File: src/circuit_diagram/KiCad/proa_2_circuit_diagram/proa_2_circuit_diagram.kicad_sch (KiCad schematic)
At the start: 29 parts, among them U1 BUCK_48V_24V_10A, U2 BUCK_24V_5V_5A, U3 ADS1115IDGS, U5 TCA9800

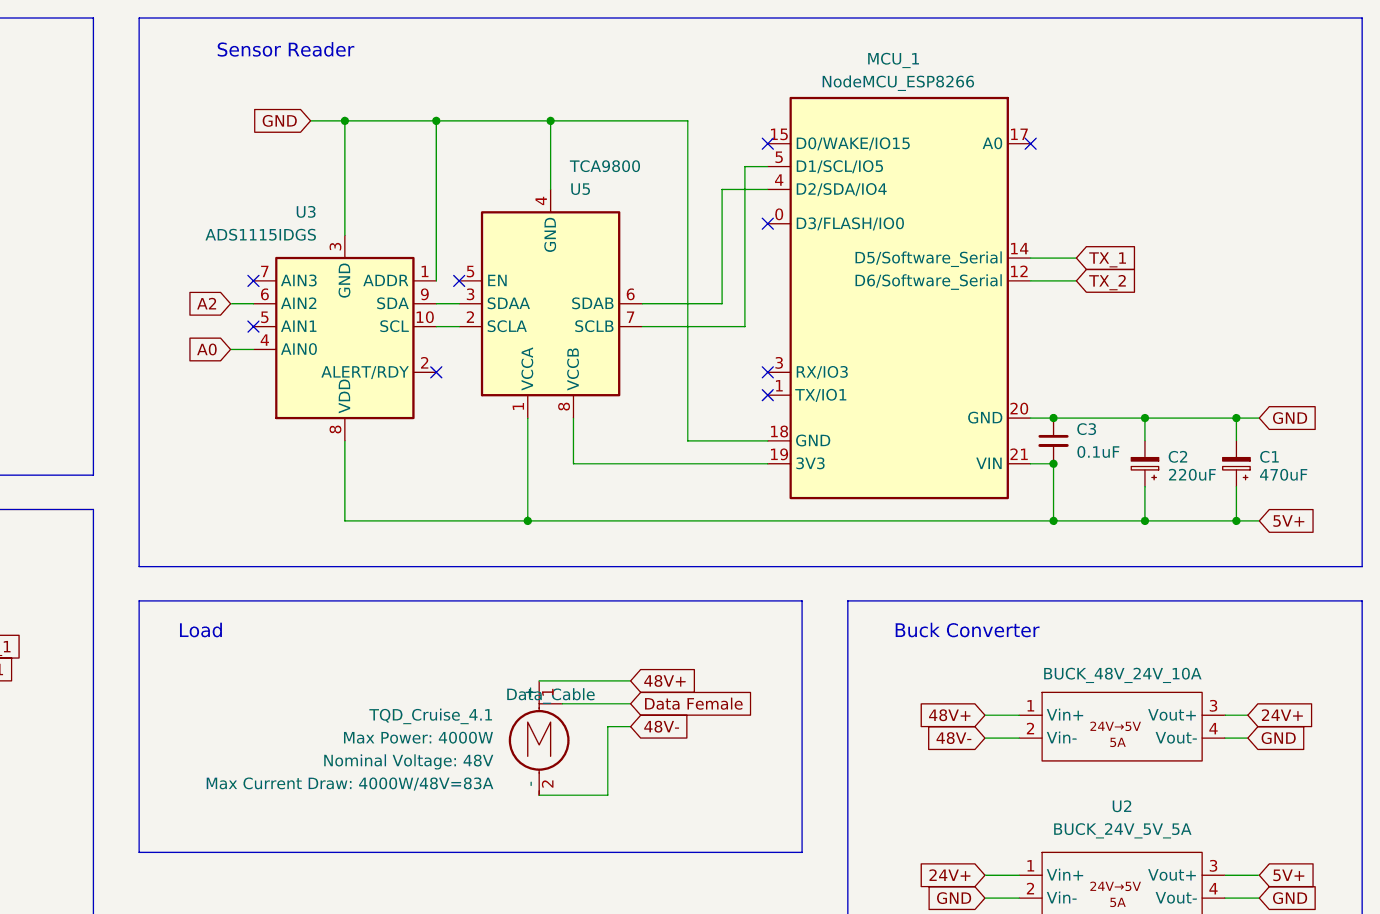
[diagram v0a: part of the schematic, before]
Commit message: Reroute electrical constant file import
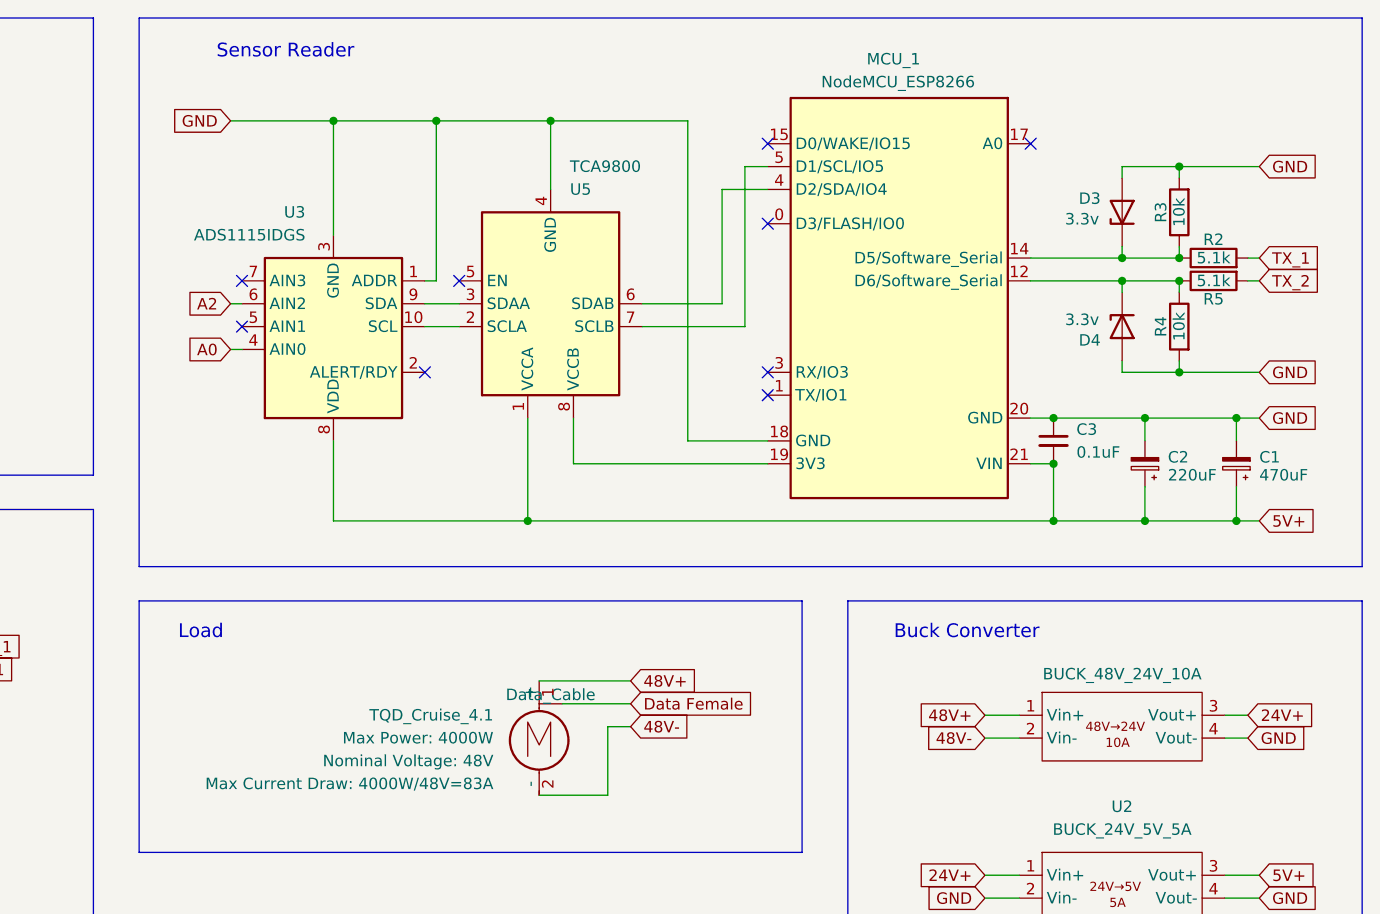
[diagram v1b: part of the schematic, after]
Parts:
- added D3, D4: 3.3v, symbol Device:D_Zener
- added R2, R5: 5.1k, symbol Device:R
- added R3, R4: 10k, symbol Device:R
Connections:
- net GND: now also D3.2 (A), D4.2 (A), R3.2, R4.2
- net TX_1: now also R2.2; no longer MCU_1.14 (D5/Software_Serial)
- net TX_2: now also R5.2; no longer MCU_1.12 (D6/Software_Serial)
- new net: D3.1 (K), MCU_1.14 (D5/Software_Serial), R2.1, R3.1
- new net: D4.1 (K), MCU_1.12 (D6/Software_Serial), R4.1, R5.1
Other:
- moved on the sheet: U3
